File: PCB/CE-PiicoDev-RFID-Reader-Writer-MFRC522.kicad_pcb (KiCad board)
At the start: 2 copper layers, 25.4 x 52 mm, 64 parts, among them J1 , J2 , J3 Conn_PiicoDev_header_01x04_Ma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, J4 Conn_01x01_Male, J5 Conn_01x01_Male, Q1 BSS138, U1 MFRC522, Y1 27.12MHz 12pF

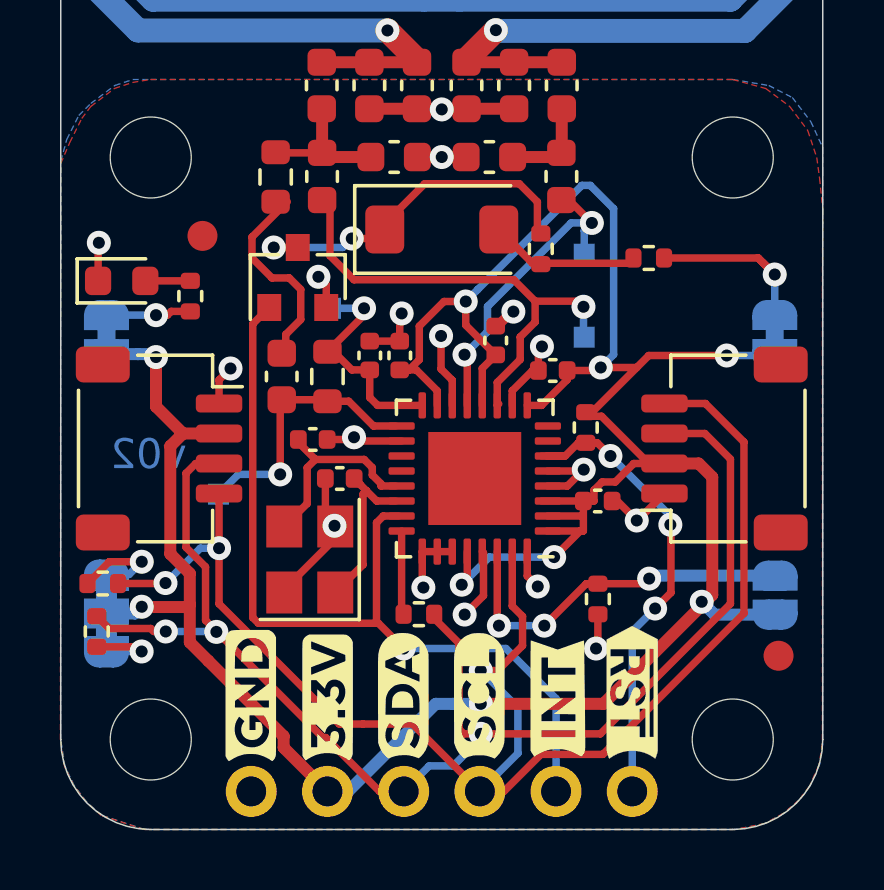
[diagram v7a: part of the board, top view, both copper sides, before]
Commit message: Remove Interrupt LED and add DIP switches
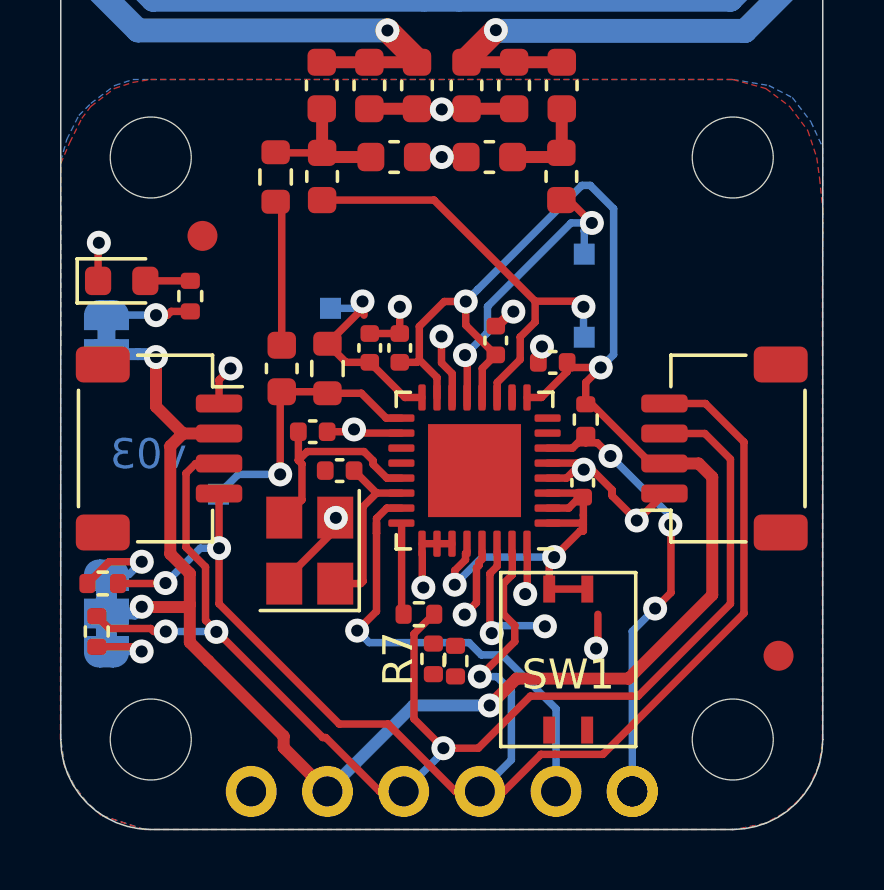
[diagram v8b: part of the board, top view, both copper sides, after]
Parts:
- removed D2: LED, CoreElectronics_Components:LED_1206_3216Metric_ReverseMount_Hole1.8x2.4mm
- removed G4: Label_PCB_Art, PiicoDev RFID MFRC522:Label_Reset_Bar_Reverse Arrow
- removed G5: Label_PCB_Art, PiicoDev RFID MFRC522:Label_Reset_Bar
- removed J5: Conn_01x01_Male, CoreElectronics_Components:PiicoDev_header_1pin_INT_uninverted
- removed JP3: SolderJumper_2_Bridged, CoreElectronics_Components:SolderJumper-2_P1.3mm_Bridged_RoundedPad1.0x1.5mm
- removed JP4: SolderJumper_2_Open, CoreElectronics_Components:SolderJumper-2_P1.3mm_Open_RoundedPad1.0x1.5mm
- removed Q1: BSS138, Package_TO_SOT_SMD:SOT-23
- removed R10, R8: 4k7, Resistor_SMD:R_0402_1005Metric
- added R7: 10k, Resistor_SMD:R_0402_1005Metric, F.Cu at (97.0, 108.4)
- added SW1: SW_DIP_x02, CoreElectronics_Components:SW_DIP_x02_Slide_CHS-02A1, F.Cu at (101.5, 108.4)
- added kibuzzard-61B8280C: G***, label, B.Cu at (90.9, 110.2)
- added kibuzzard-61B82819: G***, label, B.Cu at (93.5, 110.3)
- added kibuzzard-61B82827: G***, label, B.Cu at (96.0, 110.0)
- added kibuzzard-61B82831: G***, label, B.Cu at (98.6, 110.0)
- added kibuzzard-61B8283F: G***, label, B.Cu at (101.1, 110.4)
- added kibuzzard-61B82849: G***, label, B.Cu at (103.6, 110.3)
- J3: value Conn_PiicoDev_header_01x04_Male -> Conn_01x06_Male; footprint CoreElectronics_Components:PiicoDev_header_4pin -> CoreElectronics_Components:PiicoDev_header_6pin; moved to F.Cu
- moved R6 5.18 mm to (97.7, 108.4), turned to 90 degrees
- moved C14 0.79 mm to (102.0, 102.5), turned to 90 degrees
- moved Y1 0.30 mm to (92.9, 104.7)
- moved C12 0.27 mm to (101.0, 98.5)
- moved C2 0.27 mm to (91.9, 98.7)
- moved R4 0.27 mm to (93.5, 98.7)
- moved R9 0.27 mm to (102.1, 100.4)
- moved U1 0.26 mm to (98.4, 102.1)
- moved C4 0.26 mm to (93.9, 102.1)
- moved C1 0.26 mm to (93.0, 100.8)
- moved C13 0.25 mm to (95.9, 98.0)
- moved C3 0.25 mm to (94.9, 98.0)
- turned J3 to 90 degrees
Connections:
- U1 pad 29: GND -> Net-(R7-Pad1)
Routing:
- net /INT: track 29.1 -> 15.8 mm
- net Net-(D2-Pad1): track 11.8 -> 0.00 mm, vias 2 -> 0
- net +3V3: track 97.5 -> 88.1 mm, vias 9 -> 7
- net Net-(R6-Pad1): track 12.4 -> 4.73 mm, vias 3 -> 2
- net Net-(JP3-Pad2): track 6.63 -> 0.00 mm, vias 1 -> 0
- net Net-(D2-Pad2): track 6.16 -> 0.00 mm
- net GND: track 38.5 -> 32.4 mm, vias 17 -> 15
- net Net-(R7-Pad1): track 0.00 -> 2.34 mm, vias 0 -> 1
- net Net-(C2-Pad1): track 6.75 -> 4.87 mm
- net Net-(L1-Pad1): track 16.2 -> 15.2 mm
- net /~RST: track 16.2 -> 15.3 mm
- net Net-(C2-Pad2): track 8.92 -> 9.46 mm
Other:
- board text added: "v03"
- board text removed: "INT LED"
- board text removed: "v02"
